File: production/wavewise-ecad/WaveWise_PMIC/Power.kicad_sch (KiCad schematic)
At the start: 19 parts, among them IC1 LV14360PDDAR, U1 LM2576HVS-5.0_NOPB

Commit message: adding more to root page and updating for battery sensing
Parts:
- removed D3: SBR10200CTL-13, ZLDO1117K50TC, symbol SBR10200CTL-13:SBR10200CTL-13
- added C3: 100u/80V, Capacitor_SMD:C_1206_3216Metric_Pad1.33x1.80mm_HandSolder, symbol Device:C_Polarized_US
- added C7: 1000u/25V, Wavewise Footprints UnChecked:1000uF_10V_Cap, symbol Device:C_Polarized_US
- added D3: 1N5822, Diode_THT:D_DO-201AD_P15.24mm_Horizontal, symbol Diode:1N5822
- added D4: SBRD10200TR, Diode_THT:D_DO-201AD_P15.24mm_Horizontal, symbol Diode:1N5822
- added L2: 100u, Inductor_SMD:L_12x12mm_H6mm, symbol Device:L
- added U2: LM2576HVS-12.0_NOPB, Package_TO_SOT_SMD:TO-263-5_TabPin3, symbol LM2576S-12_NOPB:LM2576S-12_NOPB
- C1: footprint Capacitor_THT:CP_Radial_D12.5mm_P5.00mm -> Capacitor_SMD:C_1206_3216Metric_Pad1.33x1.80mm_HandSolder
- C9: footprint Capacitor_THT:CP_Radial_D8.0mm_P5.00mm -> Wavewise Footprints UnChecked:100uF_80V_Cap
- R1, R2, R3, R4: footprint Resistor_SMD:R_1206_3216Metric_Pad1.30x1.75mm_HandSolder -> (none)
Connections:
- net +48V: now also C3.P, U2.1 (VIN)
- net GND: now also C3.N, C7.N, D3.2 (A), D4.2 (A), U2.3 (GND), U2.5 (ON/OFF), U2.6 (GND)
- net at C5.2, IC1.8 (SW), L3.1: now also D4.1 (K)
- new net: D3.1 (K), L2.1, U2.2 (OUT)
- new net +12V: C7.P, L2.2, U2.4 (FB)
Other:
- note added: "Buck Converter (48V - 12V)"
- moved on the sheet: C4, C5, C8, C9, IC1, L3, R5, R6, R9

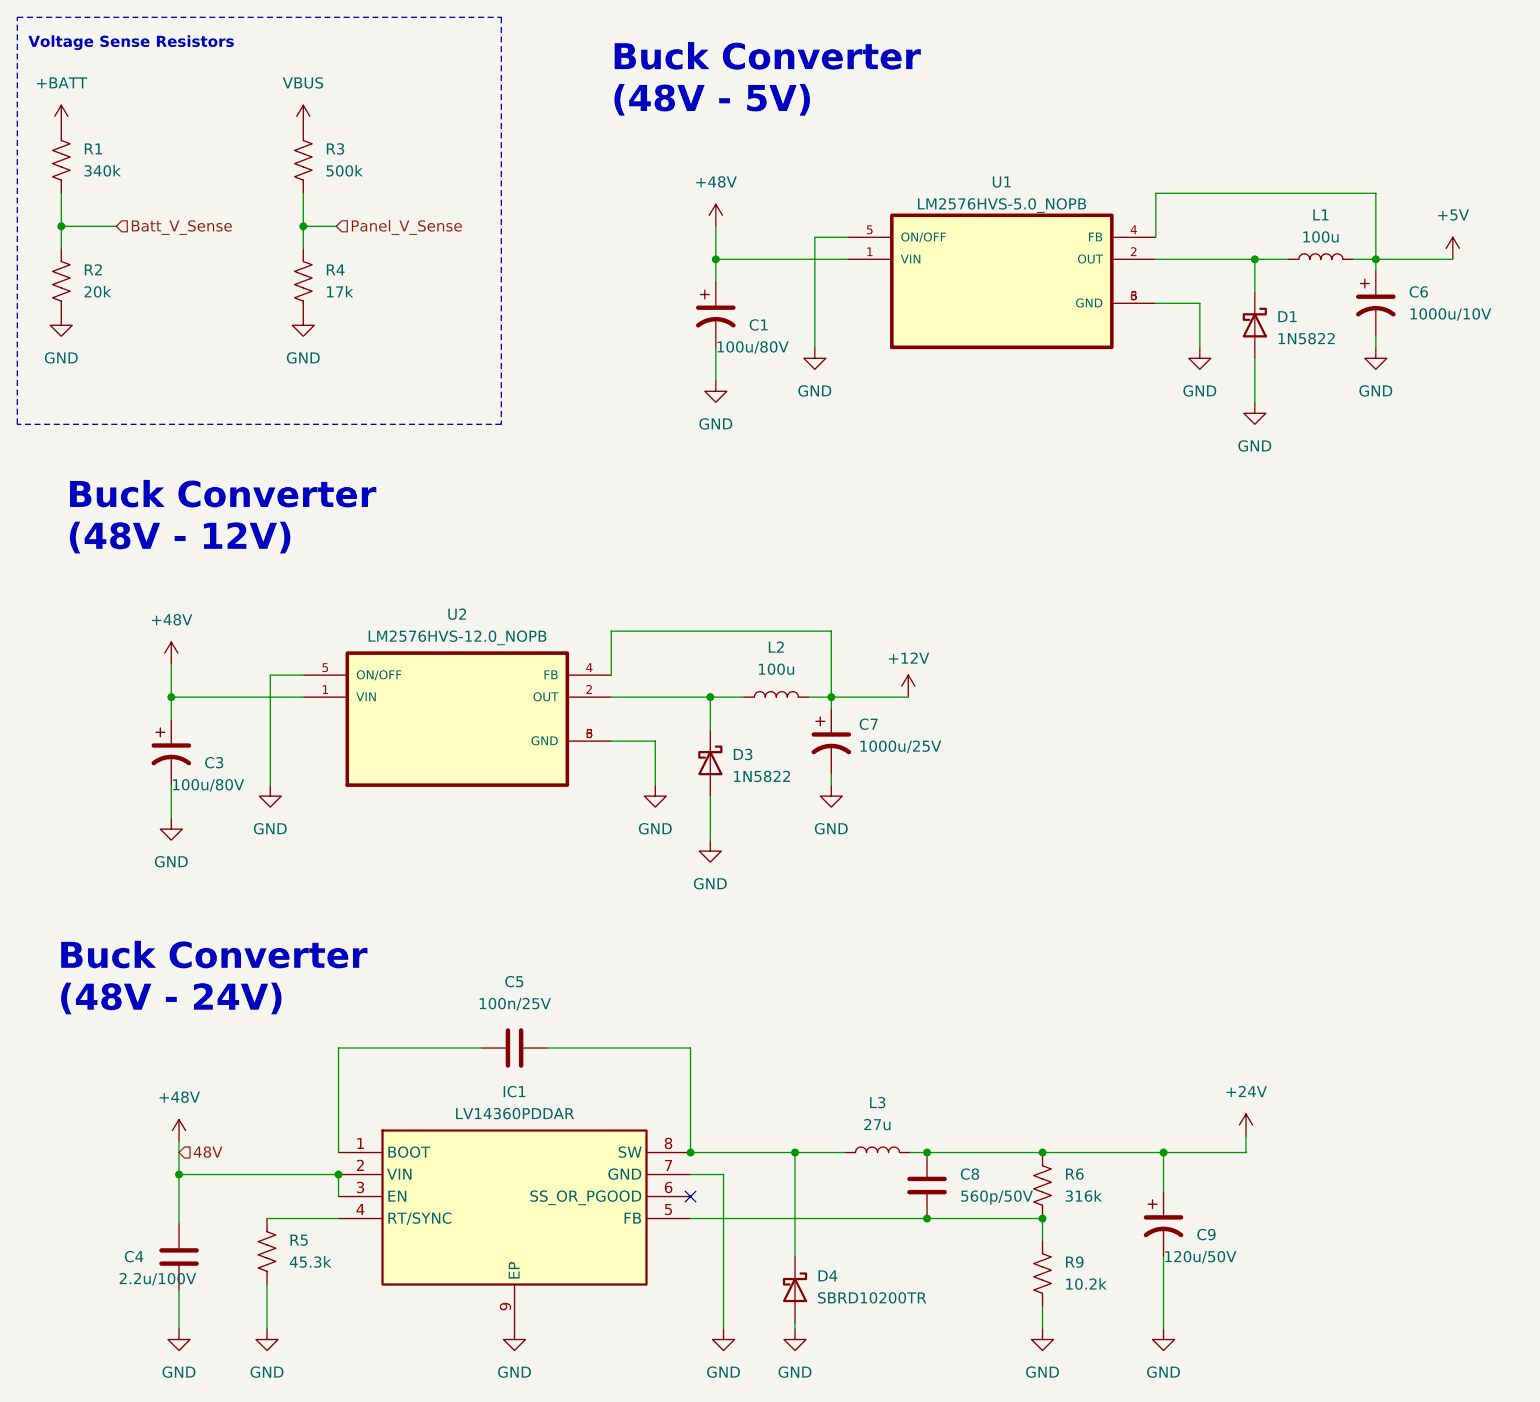
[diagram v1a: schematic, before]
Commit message: added most footprints still need polulu footprint
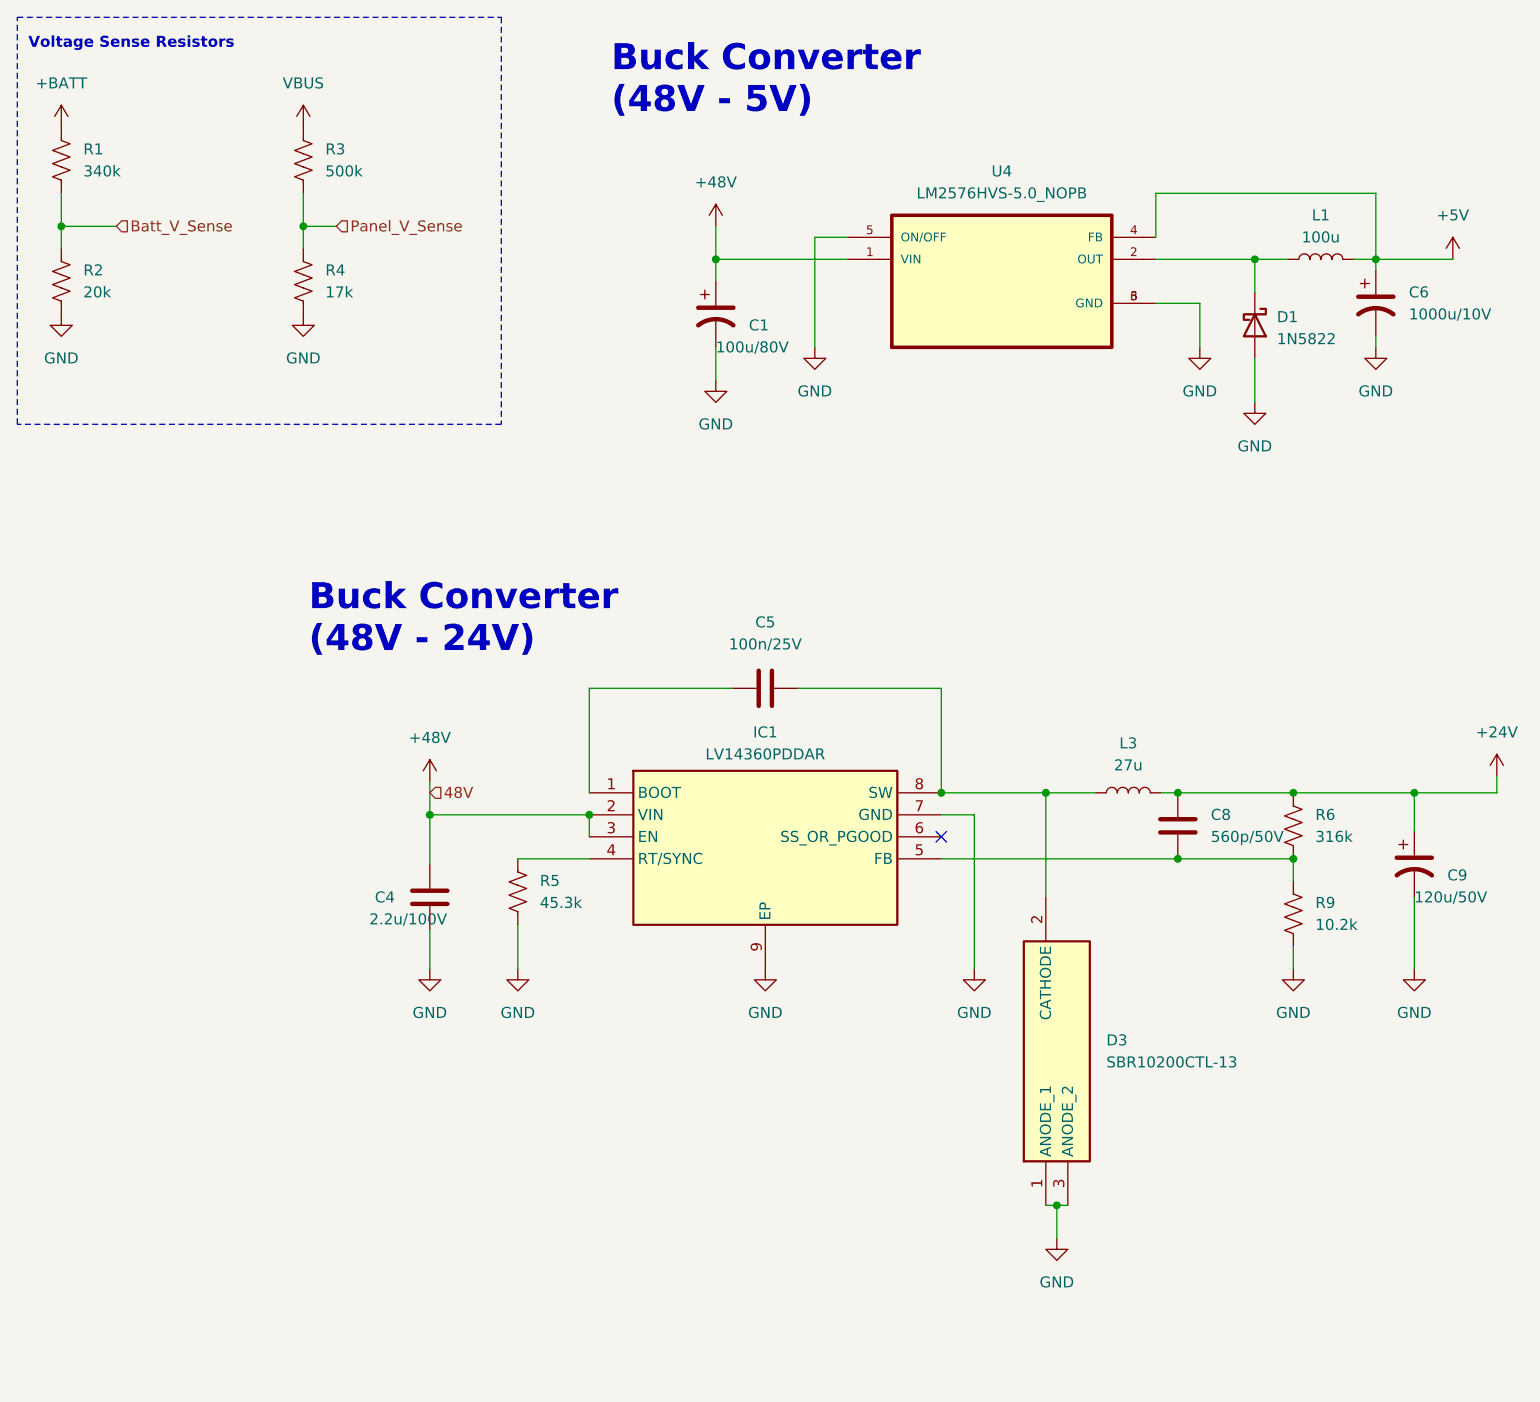
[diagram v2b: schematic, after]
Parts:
- removed C3: 100u/80V, Capacitor_SMD:C_1206_3216Metric_Pad1.33x1.80mm_HandSolder, symbol Device:C_Polarized_US
- removed C7: 1000u/25V, Wavewise Footprints UnChecked:1000uF_10V_Cap, symbol Device:C_Polarized_US
- removed D3: 1N5822, Diode_THT:D_DO-201AD_P15.24mm_Horizontal, symbol Diode:1N5822
- removed D4: SBRD10200TR, Diode_THT:D_DO-201AD_P15.24mm_Horizontal, symbol Diode:1N5822
- removed L2: 100u, Inductor_SMD:L_12x12mm_H6mm, symbol Device:L
- removed U2: LM2576HVS-12.0_NOPB, Package_TO_SOT_SMD:TO-263-5_TabPin3, symbol LM2576S-12_NOPB:LM2576S-12_NOPB
- added D3: SBR10200CTL-13, ZLDO1117K50TC, symbol SBR10200CTL-13:SBR10200CTL-13
- C1: footprint Capacitor_SMD:C_1206_3216Metric_Pad1.33x1.80mm_HandSolder -> Capacitor_THT:CP_Radial_D10.0mm_P5.00mm
- C6: footprint Wavewise Footprints UnChecked:1000uF_10V_Cap -> Capacitor_THT:CP_Radial_D10.0mm_P5.00mm
- C9: footprint Wavewise Footprints UnChecked:100uF_80V_Cap -> Capacitor_THT:CP_Radial_D8.0mm_P5.00mm
- R1, R2, R3, R4, R9: footprint (none) -> Resistor_SMD:R_0805_2012Metric_Pad1.20x1.40mm_HandSolder
- renumbered U1 to U4
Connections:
- net GND: now also D3.1 (ANODE_1), D3.3 (ANODE_2)
- net at C5.2, IC1.8 (SW), L3.1: now also D3.2 (CATHODE)
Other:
- note removed: "Buck Converter (48V - 12V)"
- moved on the sheet: C4, C5, C8, C9, IC1, L3, R5, R6, R9

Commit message: More stuff done to PCB Added polulu
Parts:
- added TP4: 24V TP, TestPoint:TestPoint_Loop_D1.80mm_Drill1.0mm_Beaded, symbol Connector:TestPoint
- added TP5: 5V TP, TestPoint:TestPoint_Loop_D1.80mm_Drill1.0mm_Beaded, symbol Connector:TestPoint
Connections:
- net +24V: now also TP4.1
- net +5V: now also TP5.1
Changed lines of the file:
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@@
   (junction (at 160.02 102.235) (diameter 0) (color 0 0 0 0)
   )
+  (junction (at 169.545 33.02) (diameter 0) (color 0 0 0 0)
+  )
   (junction (at 146.685 109.855) (diameter 0) (color 0 0 0 0)
   )
@@
   (junction (at 155.575 40.64) (diameter 0) (color 0 0 0 0)
   )
+  (junction (at 168.91 102.235) (diameter 0) (color 0 0 0 0)
+  )
   (junction (at 132.715 149.86) (diameter 0) (color 0 0 0 0)
   )
@@
   )
   (no_connect (at 119.38 107.315))
-  (wire (pts (xy 173.99 102.235) (xy 160.02 102.235))
+  (wire (pts (xy 173.99 102.235) (xy 168.91 102.235))
     (stroke (width 0) (type default))
   )
@@
   )
   (wire (pts (xy 45.72 33.02) (xy 45.72 36.83))
+    (stroke (width 0) (type default))
+  )
+  (wire (pts (xy 168.91 102.235) (xy 160.02 102.235))
     (stroke (width 0) (type default))
   )
@@
         (path "/8343c01b-8940-4cb8-a17d-91fd7fb1cccd/9b950372-21a2-4bba-abe5-3376787348cc"
           (reference "L1") (unit 1)
+        )
+      )
+    )
+  )
+  (symbol (lib_id "Connector:TestPoint") (at 168.91 102.235 0) (unit 1)
+    (in_bom yes) (on_board yes) (dnp no) (fields_autoplaced)
+    (property "Reference" "TP4" (at 171.45 97.663 0)
+      (effects (font (size 1.27 1.27)) (justify left))
+    )
+    (property "Value" "24V TP" (at 171.45 100.203 0)
+      (effects (font (size 1.27 1.27)) (justify left))
+    )
+    (property "Footprint" "TestPoint:TestPoint_Loop_D1.80mm_Drill1.0mm_Beaded" (at 173.99 102.235 0)
+      (effects (font (size 1.27 1.27)) hide)
+    )
+    (property "Datasheet" "~" (at 173.99 102.235 0)
+      (effects (font (size 1.27 1.27)) hide)
+    )
+    (pin "1")
+    (instances
+      (project "WaveWise_PMIC"
+        (path "/8343c01b-8940-4cb8-a17d-91fd7fb1cccd/9b950372-21a2-4bba-abe5-3376787348cc"
+          (reference "TP4") (unit 1)
         )
       )
@@
         )
       )
+    )
+  )
+  (symbol (lib_id "Connector:TestPoint") (at 169.545 33.02 0) (unit 1)
+    (in_bom yes) (on_board yes) (dnp no) (fields_autoplaced)
+    (property "Reference" "TP5" (at 171.45 28.448 0)
+      (effects (font (size 1.27 1.27)) (justify left))
+    )
+    (property "Value" "5V TP" (at 171.45 30.988 0)
+      (effects (font (size 1.27 1.27)) (justify left))
+    )
+    (property "Footprint" "TestPoint:TestPoint_Loop_D1.80mm_Drill1.0mm_Beaded" (at 174.625 33.02 0)
+      (effects (font (size 1.27 1.27)) hide)
+    )
+    (property "Datasheet" "~" (at 174.625 33.02 0)
+      (effects (font (size 1.27 1.27)) hide)
+    )
+    (pin "1")
+    (instances
+      (project "WaveWise_PMIC"
+        (path "/8343c01b-8940-4cb8-a17d-91fd7fb1cccd/9b950372-21a2-4bba-abe5-3376787348cc"
+          (reference "TP5") (unit 1)
+        )
+      )

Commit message: Prelim board layout
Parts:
- C5: footprint Capacitor_SMD:C_0402_1005Metric_Pad0.74x0.62mm_HandSolder -> Capacitor_SMD:C_0805_2012Metric_Pad1.18x1.45mm_HandSolder
- D3: footprint ZLDO1117K50TC -> Unchecked:TO-252DPAK_DIO
- IC1: footprint SOIC127P600X170-9N -> Package_SO:SOIC-8-1EP_3.9x4.9mm_P1.27mm_EP2.41x3.3mm_ThermalVias
- U4: footprint Package_TO_SOT_SMD:TO-263-5_TabPin3 -> Package_TO_SOT_SMD:TO-263-5_TabPin6
- renumbered TP4 to 24V_1, TP5 to 5V1
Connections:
- net +24V: now also C9.1; no longer C9.P
- net +48V: now also C1.1; no longer C1.P
- net +5V: now also C6.1; no longer C6.P
- net GND: now also C1.2, C6.2, C9.2; no longer C1.N, C6.N, C9.N
